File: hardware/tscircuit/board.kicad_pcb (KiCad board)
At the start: 2 copper layers, 240 x 180 mm, 133 parts, among them SW1 10mΩ, SW11 10mΩ, SW12 10mΩ, SW13 10mΩ

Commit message: hw(power/buses): fix 8 issues from schematic self-review (1 blocker)
An adversarial multi-agent review of the merged schematic surfaced 8 real
defects; each was verified against the combined netlist, then fixed:

- BLOCKER: +3V3 buck was TLV62569 (Vin max 5.5V) sitting on the 8.4V BAT node
  -> swapped to wide-Vin MP2315 (FB R3 45.3k->31.6k for 0.8V ref); EN auto-on
  via a 100k/47k divider off BAT instead of raw 8.4V on the EN pin.
- +5V and +3V3 MP2315 bootstrap caps (BST->SW) were missing -> bucks would not
  switch; added Cbst4 / Cbst5 100nF.
- S3 had no EN pin wired -> the reset chain (SW11 + RC) was a floating island;
  added U10.EN and connected net.S3_EN.
- C5 EN had no pull-up/RC -> undefined reset; added 10k + 1uF.
- USB VBUS missing bulk cap + TVS; added Cvbus 10uF + D1.
- RAIL_EN_5V / RAIL_EN_3V3A had no default state -> added 100k pull-downs (off).
- I2C had two pull-up pairs (~2.35k) -> removed the c5-buses pair, kept R40/R41.
- Grove ESD refdes off-by-one -> D40/D41 per the doc.

board.tsx re-merged (141 parts); power.md + power.ru.md synced.

Co-Authored-By: Claude Opus 4.8 <noreply@anthropic.com>
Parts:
- removed D40s: 10mΩ, tscircuit:resistor_res0603
- removed R_SCL, R_SDA: 4.7kΩ, tscircuit:resistor_res0402
- added C_C5EN: 1uF, tscircuit:capacitor_cap0402, F.Cu at (94.0, 110.7)
- added Cbst4: 100nF, tscircuit:capacitor_cap0402, F.Cu at (86.7, 76.1)
- added Cbst5: 100nF, tscircuit:capacitor_cap0402, F.Cu at (77.8, 74.6)
- added Cvbus: 10uF, tscircuit:capacitor_cap0805, F.Cu at (111.7, 121.0)
- added D1: 1MΩ, tscircuit:resistor_res0603, F.Cu at (115.1, 121.0)
- added D40: , tscircuit:chip_sot23-3, F.Cu at (79.8, 66.3)
- added R_C5EN: 10kΩ, tscircuit:resistor_res0402, F.Cu at (93.5, 108.3)
- added R_EN3H: 100kΩ, tscircuit:resistor_res0402, F.Cu at (72.9, 77.7)
- added R_EN3L: 47kΩ, tscircuit:resistor_res0402, F.Cu at (71.9, 80.5)
- added R_RE3A: 100kΩ, tscircuit:resistor_res0402, F.Cu at (106.2, 67.4)
- added R_RE5: 100kΩ, tscircuit:resistor_res0402, F.Cu at (94.1, 66.8)
- D42: value (none) -> 10mΩ; footprint tscircuit:chip_sot23-3 -> tscircuit:resistor_res0603
- R3: value 45.3kΩ -> 31.6kΩ
- moved D42 63.1 mm to (126.9, 103.9)
- moved Cd25 60.6 mm to (125.8, 75.4), turned to 0 degrees
- moved Cb22 56.6 mm to (126.5, 79.1)
- moved Cd23 56.4 mm to (123.4, 77.6)
- moved Cb25 53.1 mm to (120.4, 74.8), turned to -90 degrees
- moved Cd21 52.7 mm to (123.4, 80.5), turned to 90 degrees
- moved Cd22 52.2 mm to (121.0, 78.5), turned to 180 degrees
- moved Csd2 51.2 mm to (100.4, 124.6), turned to 180 degrees
- moved Cin3 45.9 mm to (91.9, 120.7)
- moved Cin5 44.5 mm to (95.6, 120.0), turned to 0 degrees
- moved Cd20 42.5 mm to (92.0, 110.7)
- moved Cjk2 34.9 mm to (97.9, 62.3), turned to 0 degrees
- moved SW13 32.3 mm to (100.0, 100.0)
- moved Cbulk31 31.9 mm to (68.9, 81.9), turned to -90 degrees
- moved Cvcc32 29.2 mm to (65.7, 76.9), turned to 90 degrees
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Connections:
- D42 pad 1: I2C_SDA -> V3V3
- D42 pad 2: I2C_SCL -> V_BCKP
- U10 pad 41: (no net) -> S3_EN
- U4 pad 1: (no net) -> .Cbst4 > .pin1 to .U4 > .BST
- U5 pad 1: .U5 > .SW to .L3 > .pin1 -> .Cbst5 > .pin1 to .U5 > .BST
- U5 pad 2: GND -> BAT
- U5 pad 3: .R3 > .pin2 to .U5 > .FB -> .U5 > .SW to .L3 > .pin1
- U5 pad 4: BAT -> GND
- U5 pad 5: BAT -> .R3 > .pin2 to .U5 > .FB
- U5 pad 6: (no net) -> .R_EN3H > .pin2 to .U5 > .EN
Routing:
- net GND: track 512.6 -> 0.00 mm, vias 50 -> 0
- net V3V3: track 321.6 -> 0.00 mm, vias 40 -> 0
- net V5: track 115.7 -> 0.00 mm, vias 12 -> 0
- net I2C_SDA: track 105.2 -> 0.00 mm, vias 14 -> 0
- net I2C_SCL: track 83.9 -> 0.00 mm, vias 14 -> 0
- net CC1101_RF: track 79.9 -> 0.00 mm, vias 4 -> 0
- net BAT: track 77.9 -> 0.00 mm, vias 12 -> 0
- net SPK_P: track 67.9 -> 0.00 mm, vias 2 -> 0
- net SPI_SCK: track 64.1 -> 0.00 mm, vias 12 -> 0
- net SPI_MOSI: track 63.8 -> 0.00 mm, vias 6 -> 0
- net SPI_MISO: track 62.6 -> 0.00 mm, vias 4 -> 0
- net GPS_UART_RX: track 57.0 -> 0.00 mm, vias 6 -> 0
- net .Cjk2 > .pin2 to .J30 > .R: track 46.5 -> 0.00 mm, vias 6 -> 0
- net LoRa_BUSY: track 45.3 -> 0.00 mm, vias 6 -> 0
- net nRF24_CE: track 45.2 -> 0.00 mm, vias 8 -> 0
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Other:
- board size 240 x 180 mm -> 250 x 180 mm

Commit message: hw(board): merge all 6 realized sheets into one real-parts board (169 parts)
Final recombine with the parts engine on: every sheet's real jlcpcb: footprints
carried into one board.tsx. Cross-sheet nets stitch (SPI / I2C / rails / CS /
interrupts / C5-link / SP4T-select all verified in board.net). KiCad DRC:
schematic_parity = 0, 0 shorts, 0 NaN. Refdes collisions renamed (U20, Y1, and the
new Rbias). The board is not yet routed (0 copper) — unconnected_items is the
ratsnest, not breaks; routing (RF by hand) is the next step. README updated.

Co-Authored-By: Claude Opus 4.8 <noreply@anthropic.com>
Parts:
- removed the D53 at (133.0, 92.6)
- removed the D54 at (69.5, 95.2)
- removed Rbias: 4.7kΩ, tscircuit:resistor_res0402
- removed the Rd52 at (133.6, 81.4)
- removed the Rd53 at (131.4, 94.8)
- added Cbat: 10uF, tscircuit:capacitor_cap0805, F.Cu at (65.2, 147.2)
- added Cbtst: 47nF, tscircuit:capacitor_cap0402, F.Cu at (77.7, 125.1)
- added Cbulk40: 10uF, tscircuit:capacitor_cap0805, F.Cu at (100.0, 100.0)
- added Cdc, Cds1, Cio40, Cu51, Cvcc40, Cvdd30b: 100nF, tscircuit:capacitor_cap0402, F.Cu at (100.0, 100.0)
- added Cpmid: 10uF, tscircuit:capacitor_cap0805, F.Cu at (124.0, 123.0)
- added Cregn: 4.7uF, tscircuit:capacitor_cap0805, F.Cu at (87.7, 149.1)
- added Csns: 47uF, tscircuit:capacitor_cap1210, F.Cu at (120.3, 130.8)
- added Cvbusic: 1uF, tscircuit:capacitor_cap0402, F.Cu at (115.8, 100.6)
- added Cvc: 0.1uF, tscircuit:capacitor_cap0402, F.Cu at (100.6, 163.5)
- added Cvcc4: 0.1uF, tscircuit:capacitor_cap0402, F.Cu at (80.4, 144.7)
- added Cvcc5: 0.1uF, tscircuit:capacitor_cap0402, F.Cu at (81.3, 157.7)
- added Cvdd: 0.1uF, tscircuit:capacitor_cap0402, F.Cu at (93.8, 165.5)
- added Q2: , tscircuit:chip, F.Cu at (93.0, 169.5)
- added Raam4: 100kΩ, tscircuit:resistor_res0402, F.Cu at (67.9, 142.1)
- added Raam5: 100kΩ, tscircuit:resistor_res0402, F.Cu at (57.6, 142.1)
- added Rcbset: 10Ω, tscircuit:resistor_res0402, F.Cu at (89.6, 137.0)
- added Ren: 10kΩ, tscircuit:resistor_res0402, F.Cu at (100.0, 100.0)
- added Rilim: 383Ω, tscircuit:resistor_res0402, F.Cu at (87.2, 137.0)
- added Rmid: 300Ω, tscircuit:resistor_res0402, F.Cu at (83.7, 156.2)
- added Rts_top: 5.23kΩ, tscircuit:resistor_res0402, F.Cu at (84.3, 137.0)
- added Rvc: 470Ω, tscircuit:resistor_res0402, F.Cu at (92.2, 163.1)
- added Rvdd: 470Ω, tscircuit:resistor_res0402, F.Cu at (81.3, 155.8)
- added Rvm: 2kΩ, tscircuit:resistor_res0402, F.Cu at (96.7, 168.1)
- added SW11, SW12, SW13: 10mΩ, tscircuit:resistor_res1210, F.Cu at (100.0, 100.0)
- added a_Rbias: 4.7kΩ, tscircuit:resistor_res0402, F.Cu at (100.0, 100.0)
- added rf_Rbias: 56kΩ, tscircuit:resistor_res0402, F.Cu at (100.0, 100.0)
- BL1: footprint tscircuit:chip_soic8 -> tscircuit:chip_soic6
- BT1: footprint tscircuit:chip_soic8 -> tscircuit:chip_pinrow3
- BT40: value 100000uF -> (none); footprint tscircuit:capacitor_cap1210 -> tscircuit:chip
- D40, D41: footprint tscircuit:chip_sot23-3 -> tscircuit:chip
- D42: value 10mΩ -> (none); footprint tscircuit:resistor_res0603 -> tscircuit:chip
- D53: renamed from Ren; value 10kΩ -> LED; footprint tscircuit:resistor_res0402 -> tscircuit:led_0603
- D54: renamed from SW13; value 10mΩ -> LED; footprint tscircuit:resistor_res1210 -> tscircuit:led_0603
- DS1, SW10, U27, U51: footprint tscircuit:chip_sot23-5 -> tscircuit:chip
- J1, J2, J40, J41, J50, Q1, U3, U4, U40, U5, U6: footprint tscircuit:chip_soic8 -> tscircuit:chip
- J30: footprint tscircuit:chip_soic8 -> tscircuit:chip_pinrow4
- Q50, Q51, Q52, Q53, Q54, Q55, Q56, Q57, Q58, U50: footprint tscircuit:chip_sot23 -> tscircuit:chip
- Rd52: renamed from SW11; value 10mΩ -> 4.7kΩ; footprint tscircuit:resistor_res1210 -> tscircuit:resistor_res0402
- Rd53: renamed from SW12; value 10mΩ -> 4.7kΩ; footprint tscircuit:resistor_res1210 -> tscircuit:resistor_res0402
- U10: footprint tscircuit:chip_qfn48 -> tscircuit:chip
- U11, U2, U23, U24, U25, U30, U31, m_U20: footprint tscircuit:chip_soic16 -> tscircuit:chip
- U12, U13: footprint tscircuit:chip_ssop24 -> tscircuit:chip
- U21, U22, rf_U20: footprint tscircuit:chip_soic8 -> tscircuit:chip_pinrow8_p2.54_doublerow
- U28, U32, U33: footprint tscircuit:chip_sot23-6 -> tscircuit:chip
- a_Y1: value 1mΩ -> (none); footprint tscircuit:resistor_res0402 -> tscircuit:chip
- rf_Y1: footprint tscircuit:crystal_cd3215 -> tscircuit:crystal_crystal_3215_2
- moved Q52 102.4 mm to (65.2, 163.3)
- moved D41 101.9 mm to (70.0, 163.4), turned to 0 degrees
- moved D40 98.7 mm to (88.5, 164.6), turned to -90 degrees
- moved Q53 98.2 mm to (64.3, 158.8)
- moved J41 95.9 mm to (79.4, 167.5), turned to 0 degrees
- moved U44 86.5 mm to (82.8, 151.5), turned to 180 degrees
- moved R3 85.0 mm to (84.2, 158.6), turned to 180 degrees
- moved J40 84.8 mm to (73.0, 154.3), turned to -90 degrees
- moved L3 82.0 mm to (64.5, 152.2), turned to -90 degrees
- moved R2 81.1 mm to (72.7, 146.3)
- moved Cout3a 81.0 mm to (45.0, 122.4), turned to 180 degrees
- moved R_RE3A 78.3 mm to (44.9, 116.1), turned to 180 degrees
- moved U22 76.5 mm to (97.4, 159.8), turned to 0 degrees
- moved BT1 75.1 mm to (79.4, 176.1), turned to 0 degrees
- moved R4 74.7 mm to (61.0, 150.4), turned to 180 degrees
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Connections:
- net .R_EN3H > .pin2 to .U5 > .EN renamed .R_EN3H > .pin2 to .U5 > .pin6
- BL1 pad 1: .U23 > .RFP to .BL1 > .RFP -> .U23 > .RF_P to .BL1 > .RFP
- BL1 pad 2: .U23 > .RFN to .BL1 > .RFN -> .U23 > .RF_N to .BL1 > .RFN
- BL1 pad 5: (no net) -> GND
- BL1 pad 6: (no net) -> GND
- BT1 pad 3: .BT1 > .P_MINUS to .Q1 > .D -> BMINUS
- CL1 pad 1: .U30 > .RCLK to .a_Y1 > .pin1 -> .U30 > .RCLK to .a_Y1 > .OSC1
- CL2 pad 1: GND -> .U30 > .RCLK to .a_Y1 > .OSC1
- Cx1 pad 1: .U23 > .XOSC1 to .rf_Y1 > .pin1 -> .U23 > .XOSC_Q1 to .rf_Y1 > .pin1
- Cx2 pad 1: .U23 > .XOSC2 to .rf_Y1 > .pin2 -> .U23 > .XOSC_Q2 to .rf_Y1 > .pin2
- D42 pad 2: V_BCKP -> (no net)
- D53 pad 1: V3V3 -> .D53 > .pin1 to .Rd53 > .pin1
- D53 pad 2: S3_EN -> .D53 > .pin2 to .Q53 > .C
- D54 pad 1: PTT_BTN -> .D54 > .pin1 to .Rd54 > .pin1
- D54 pad 2: GND -> .D54 > .pin2 to .Q54 > .C
- J1 pad 1: VBUS_S3 -> GND
- J1 pad 3: .Rcc1 > .pin1 to .J1 > .CC1 -> GND
- J1 pad 4: .Rcc2 > .pin1 to .J1 > .CC2 -> GND
- J1 pad 5: USB_DP_S3 -> GND
- J1 pad 6: USB_DM_S3 -> VBUS_S3
- J1 pad 7: (no net) -> .Rcc2 > .pin1 to .J1 > .CC2
- J2 pad 1: VBUS_C5 -> GND
- J2 pad 3: (no net) -> GND
- J2 pad 4: (no net) -> GND
- J2 pad 5: USB_DP_C5 -> GND
- J2 pad 6: USB_DM_C5 -> VBUS_C5
- J40 pad 1: V3V3 -> GND
- J40 pad 2: GND -> V3V3
- J40 pad 5: (no net) -> GND
- J40 pad 6: (no net) -> GND
- J41 pad 1: V3V3 -> GND
- J41 pad 2: GND -> V3V3
- J41 pad 5: (no net) -> GND
- J41 pad 6: (no net) -> GND
- J50 pad 1: SD_CS -> (no net)
- J50 pad 2: SPI_MOSI -> SD_CS
- J50 pad 3: SPI_MISO -> SPI_MOSI
- J50 pad 4: SPI_SCK -> V3V3
- J50 pad 5: V3V3 -> SPI_SCK
- J50 pad 7: SD_CD -> SPI_MISO
- L1 pad 1: .U2 > .SW to .L1 > .pin1 -> PMID
- L1 pad 2: BAT -> SW
- Q1 pad 1: .U3 > .DO to .Q1 > .G1 -> .U3 > .DO to .Q1 > .G
- Q1 pad 2: .U3 > .CO to .Q1 > .G2 -> BMINUS
- Q1 pad 3: .BT1 > .P_MINUS to .Q1 > .D -> PACKMID
- R_C5S27 pad 1: .m_U20 > .STRAP27 to .R_C5S27 > .pin1 -> .m_U20 > .IO27 to .R_C5S27 > .pin1
- Rd52 pad 1: S3_EN -> .D52 > .pin1 to .Rd52 > .pin1
- Rd52 pad 2: GND -> V3V3
- Rd53 pad 1: S3_BOOT -> .D53 > .pin1 to .Rd53 > .pin1
- Rd53 pad 2: GND -> V3V3
- Rin32 pad 2: .Rin32 > .pin2 to .U32 > .IN -> .Rin32 > .pin2 to .U32 > .IN_POS
- RsumL pad 1: .U30 > .LOUT to .RsumL > .pin1 -> .U30 > .pin2 to .RsumL > .pin1
- RsumR pad 1: .U30 > .ROUT to .RsumR > .pin1 -> .U30 > .pin1 to .RsumR > .pin1
- SW10 pad 4: ENC_SW -> GND
- SW10 pad 5: GND -> ENC_SW
- U10 pad 1: S3_BOOT -> GND
- U10 pad 10: HC138_B -> SA868_UART_RX
- U10 pad 11: HC138_C -> GPS_UART_RX
- U10 pad 12: SPI_MOSI -> HC138_A
- U10 pad 13: SPI_SCK -> USB_DM_S3
- U10 pad 14: SPI_MISO -> USB_DP_S3
- U10 pad 15: LCD_DC -> LoRa_DIO1
- U10 pad 16: LoRa_BUSY -> nRF24_IRQ
- U10 pad 17: SA868_UART_TX -> HC138_B
- U10 pad 18: SA868_UART_RX -> HC138_C
- U10 pad 19: GPS_UART_RX -> SPI_MOSI
- U10 pad 2: WS2812 -> V3V3
- U10 pad 20: USB_DM_S3 -> SPI_SCK
- U10 pad 21: USB_DP_S3 -> SPI_MISO
- U10 pad 22: LCD_TE -> LCD_DC
- U10 pad 23: C5_EN -> LCD_TE
- U10 pad 24: C5_BOOT -> GPS_UART_TX
- U10 pad 25: C5LINK_SCK -> PCA9555_INT
- U10 pad 26: C5LINK_MOSI -> CC1101_GDO2
- U10 pad 27: C5LINK_MISO -> S3_BOOT
- U10 pad 28: C5LINK_CS -> C5LINK_SCK
- U10 pad 29: C5LINK_DRDY -> C5LINK_MOSI
- U10 pad 3: IR_TX -> S3_EN
- U10 pad 30: ENC_A -> C5LINK_MISO
- U10 pad 31: ENC_B -> C5LINK_CS
- U10 pad 32: IR_RX -> C5LINK_DRDY
- U10 pad 33: C5_FLASH_TX -> ENC_A
- U10 pad 34: C5_FLASH_RX -> ENC_B
- U10 pad 35: CC1101_GDO2 -> IR_RX
- U10 pad 36: nRF24_IRQ -> C5_FLASH_RX
- U10 pad 37: GPS_UART_TX -> C5_FLASH_TX
- U10 pad 38: PCA9555_INT -> IR_TX
- U10 pad 39: V3V3 -> WS2812
- U10 pad 4: LoRa_DIO1 -> I2C_SDA
- U10 pad 41: S3_EN -> GND
- U10 pad 42: (no net) -> GND
- U10 pad 43: (no net) -> GND
- U10 pad 44: (no net) -> GND
- U10 pad 45: (no net) -> GND
- U10 pad 46: (no net) -> GND
- U10 pad 47: (no net) -> GND
- U10 pad 48: (no net) -> GND
- U10 pad 5: I2C_SDA -> I2C_SCL
- U10 pad 6: I2C_SCL -> nRF24_CE
- U10 pad 7: nRF24_CE -> CC1101_GDO0
- U10 pad 8: CC1101_GDO0 -> LoRa_BUSY
- U10 pad 9: HC138_A -> SA868_UART_TX
- U12 pad 1: ENC_SW -> PCA9555_INT
- U12 pad 10: BQ_INT -> LCD_RESX
- U12 pad 11: BQ_CD -> MUX_SEL
- U12 pad 12: LoRa_TR -> GND
- U12 pad 13: PAM_SD -> BQ_INT
- U12 pad 14: LCD_BL_EN -> BQ_CD
- U12 pad 15: RFSW_A -> LoRa_TR
- U12 pad 16: HC138_EN -> PAM_SD
- U12 pad 17: SD_CD -> LCD_BL_EN
- U12 pad 18: PCA9555_INT -> RFSW_A
- U12 pad 19: I2C_SCL -> HC138_EN
- U12 pad 2: SA868_PTT -> GND
- U12 pad 20: I2C_SDA -> SD_CD
- U12 pad 22: GND -> I2C_SCL
- U12 pad 23: GND -> I2C_SDA
- U12 pad 3: SA868_PD -> GND
- U12 pad 4: Si4732_RST -> ENC_SW
- U12 pad 5: LoRa_NRESET -> SA868_PTT
- U12 pad 6: BUZZER -> SA868_PD
- U12 pad 7: LCD_RESX -> Si4732_RST
- U12 pad 8: MUX_SEL -> LoRa_NRESET
- U12 pad 9: GND -> BUZZER
- U13 pad 1: PTT_BTN -> PCA9555_INT
- U13 pad 10: (no net) -> C5_BOOT
- U13 pad 11: (no net) -> RFSW_C
- U13 pad 12: (no net) -> GND
- U13 pad 18: PCA9555_INT -> (no net)
- U13 pad 19: I2C_SCL -> (no net)
- U13 pad 2: RAIL_EN_5V -> GND
- U13 pad 20: I2C_SDA -> (no net)
- U13 pad 22: GND -> I2C_SCL
- U13 pad 23: GND -> I2C_SDA
- U13 pad 3: RAIL_EN_3V3A -> GND
- U13 pad 4: JACK_DET -> PTT_BTN
- U13 pad 5: RFSW_B -> RAIL_EN_5V
- U13 pad 6: (no net) -> RAIL_EN_3V3A
- U13 pad 7: (no net) -> JACK_DET
- U13 pad 8: (no net) -> RFSW_B
- U13 pad 9: GND -> C5_EN
- U2 pad 1: VBUS_S3 -> (no net)
- U2 pad 10: GND -> .Rcbset > .pin1 to .U2 > .CBSET
- U2 pad 11: (no net) -> .Cregn > .pin1 to .U2 > .REGN
- U2 pad 12: (no net) -> .Cbtst > .pin1 to .U2 > .BTST
- U2 pad 13: (no net) -> BAT
- U2 pad 14: (no net) -> BAT
- U2 pad 15: (no net) -> BAT
- U2 pad 16: (no net) -> BAT
- U2 pad 2: .U2 > .SW to .L1 > .pin1 -> (no net)
- U2 pad 3: BAT -> BQ_CD
- U2 pad 4: BATM -> I2C_SDA
- U2 pad 5: TS -> I2C_SCL
- U2 pad 6: I2C_SDA -> BQ_INT
- U2 pad 7: I2C_SCL -> TS
- U2 pad 8: BQ_CD -> .Rilim > .pin1 to .U2 > .ILIM
- U2 pad 9: BQ_INT -> .Rmid > .pin1 to .U2 > .MID
- U23 pad 1: V3V3 -> SPI_SCK
- U23 pad 10: .U23 > .RFN to .BL1 > .RFN -> .U23 > .XOSC_Q2 to .rf_Y1 > .pin2
- U23 pad 11: .U23 > .XOSC1 to .rf_Y1 > .pin1 -> V3V3
- U23 pad 12: .U23 > .XOSC2 to .rf_Y1 > .pin2 -> .U23 > .RF_P to .BL1 > .RFP
- U23 pad 13: (no net) -> .U23 > .RF_N to .BL1 > .RFN
- U23 pad 14: (no net) -> V3V3
- U23 pad 15: (no net) -> V3V3
- U23 pad 16: (no net) -> GND
- U23 pad 2: GND -> SPI_MISO
- U23 pad 3: CC1101_CS -> CC1101_GDO2
- U23 pad 4: SPI_SCK -> V3V3
- U23 pad 5: SPI_MOSI -> .U23 > .DCOUPL to .Cdc > .pin1
- U23 pad 6: SPI_MISO -> CC1101_GDO0
- U23 pad 7: CC1101_GDO0 -> CC1101_CS
- U23 pad 8: CC1101_GDO2 -> .U23 > .XOSC_Q1 to .rf_Y1 > .pin1
- U23 pad 9: .U23 > .RFP to .BL1 > .RFP -> V3V3
- U24 pad 1: CC1101_RF -> GND
- U24 pad 10: (no net) -> .U24 > .RF4 to .Lm915 > .pin1
- U24 pad 11: (no net) -> GND
- U24 pad 12: (no net) -> GND
- U24 pad 13: (no net) -> CC1101_RF
- U24 pad 14: (no net) -> GND
- U24 pad 15: (no net) -> GND
- U24 pad 2: .U24 > .RF1 to .Lm315 > .pin1 -> .U24 > .RF3 to .Lm868 > .pin1
- U24 pad 3: .U24 > .RF2 to .Lm433 > .pin1 -> .U24 > .RF1 to .Lm315 > .pin1
- U24 pad 4: .U24 > .RF3 to .Lm868 > .pin1 -> V3V3
- U24 pad 5: .U24 > .RF4 to .Lm915 > .pin1 -> RFSW_C
- U24 pad 6: RFSW_A -> RFSW_B
- U24 pad 7: RFSW_B -> RFSW_A
- U24 pad 8: V3V3 -> GND
- U24 pad 9: GND -> .U24 > .RF2 to .Lm433 > .pin1
- U25 pad 1: V3V3 -> GND
- U25 pad 10: LoRa_RXEN -> GND
- U25 pad 11: LoRa_TR -> GND
- U25 pad 12: ANT_LoRa -> GND
- U25 pad 13: (no net) -> LoRa_DIO1
- U25 pad 14: (no net) -> LoRa_BUSY
- U25 pad 15: (no net) -> LoRa_NRESET
- U25 pad 16: (no net) -> SPI_MISO
- U25 pad 3: LoRa_NSS -> GND
- U25 pad 4: SPI_SCK -> GND
- U25 pad 5: SPI_MOSI -> GND
- U25 pad 6: SPI_MISO -> LoRa_RXEN
- U25 pad 7: LoRa_BUSY -> LoRa_TR
- U25 pad 8: LoRa_DIO1 -> (no net)
- U25 pad 9: LoRa_NRESET -> V3V3
- U27 pad 1: LoRa_TR -> (no net)
- U27 pad 2: LoRa_RXEN -> LoRa_TR
- U27 pad 3: V3V3 -> GND
- U27 pad 4: GND -> LoRa_RXEN
- U27 pad 5: (no net) -> V3V3
- U28 pad 2: nRF24_2_IRQ -> GND
- U28 pad 3: nRF24_3_IRQ -> nRF24_2_IRQ
- U28 pad 6: GND -> nRF24_3_IRQ
- U3 pad 1: BAT -> .U3 > .DO to .Q1 > .G
- U3 pad 2: BATM -> .U3 > .CO to .Q2 > .G
- U3 pad 3: .BT1 > .P_MINUS to .Q1 > .D -> .Rvm > .pin1 to .U3 > .VM
- U3 pad 4: .U3 > .DO to .Q1 > .G1 -> .Rvc > .pin1 to .U3 > .VC
- U3 pad 5: .U3 > .CO to .Q1 > .G2 -> .Rvdd > .pin1 to .U3 > .VDD
- U3 pad 6: (no net) -> BMINUS
- U30 pad 1: V3V3A -> .U30 > .pin1 to .RsumR > .pin1
- U30 pad 10: .U30 > .LOUT to .RsumL > .pin1 -> GND
- U30 pad 11: .U30 > .ROUT to .RsumR > .pin1 -> I2C_SCL
- U30 pad 12: (no net) -> I2C_SDA
- U30 pad 13: (no net) -> .U30 > .RCLK to .a_Y1 > .OSC1
- U30 pad 14: (no net) -> V3V3A
- U30 pad 15: (no net) -> GND
- U30 pad 2: GND -> .U30 > .pin2 to .RsumL > .pin1
- U30 pad 3: I2C_SDA -> (no net)
- U30 pad 4: I2C_SCL -> (no net)
- U30 pad 5: GND -> (no net)
- U30 pad 6: Si4732_RST -> ANT_FM
- U30 pad 7: .U30 > .RCLK to .a_Y1 > .pin1 -> GND
- U30 pad 9: ANT_FM -> Si4732_RST
- U31 pad 1: V5 -> GND
- U31 pad 10: ANT_UHF -> GND
- U31 pad 12: (no net) -> ANT_UHF
- U31 pad 16: (no net) -> SA868_UART_TX
- U31 pad 2: V3V3 -> (no net)
- U31 pad 3: GND -> SA_AF
- U31 pad 4: SA868_UART_TX -> (no net)
- U31 pad 5: SA868_UART_RX -> SA868_PTT
- U31 pad 6: SA868_PTT -> SA868_PD
- U31 pad 7: SA868_PD -> (no net)
- U31 pad 8: SA_AF -> V5
- U31 pad 9: .Cmic > .pin2 to .U31 > .MIC_IN -> GND
- U32 pad 1: .Rin32 > .pin2 to .U32 > .IN -> PAM_SD
- U32 pad 2: PAM_SD -> GND
- U32 pad 3: V5 -> .Rin32 > .pin2 to .U32 > .IN_POS
- U32 pad 4: GND -> (no net)
- U32 pad 6: SPK_M -> V5
- U33 pad 1: SI_AUDIO -> SA_AF
- U33 pad 2: SA_AF -> GND
- U33 pad 3: MUX_OUT -> SI_AUDIO
- U33 pad 4: MUX_SEL -> MUX_OUT
- U33 pad 6: GND -> MUX_SEL
- U4 pad 1: .Cbst4 > .pin1 to .U4 > .BST -> .Raam4 > .pin1 to .U4 > .AAM
- U4 pad 5: .R1 > .pin2 to .U4 > .FB -> .Cbst4 > .pin1 to .U4 > .BST
- U4 pad 7: (no net) -> .Cvcc4 > .pin1 to .U4 > .VCC
- U4 pad 8: (no net) -> .R1 > .pin2 to .U4 > .FB
- U40 pad 1: V3V3 -> GND
- U40 pad 2: GND -> V3V3
- U40 pad 3: GPS_UART_RX -> V_BCKP
- U40 pad 4: GPS_UART_TX -> GND
- U40 pad 5: V_BCKP -> GND
- U40 pad 6: (no net) -> GND
- U5 pad 1: .Cbst5 > .pin1 to .U5 > .BST -> .Raam5 > .pin1 to .U5 > .AAM
- U5 pad 5: .R3 > .pin2 to .U5 > .FB -> .Cbst5 > .pin1 to .U5 > .BST
- U5 pad 7: (no net) -> .Cvcc5 > .pin1 to .U5 > .VCC
- U5 pad 8: (no net) -> .R3 > .pin2 to .U5 > .FB
- U51 pad 1: WS2812 -> GND
- U51 pad 2: .U51 > .Y to .DS1 > .DIN -> WS2812
- U51 pad 4: V5 -> .U51 > .Y to .DS1 > .DIN
- U51 pad 5: GND -> V5
- U6 pad 4: V3V3A -> (no net)
- U6 pad 5: (no net) -> V3V3A
- a_Y1 pad 1: .U30 > .RCLK to .a_Y1 > .pin1 -> .U30 > .RCLK to .a_Y1 > .OSC1
- m_U20 pad 1: C5_EN -> GND
- m_U20 pad 10: C5_FLASH_RX -> C5LINK_CS
- m_U20 pad 11: C5_FLASH_TX -> C5LINK_DRDY
- m_U20 pad 12: USB_DM_C5 -> (no net)
- m_U20 pad 13: USB_DP_C5 -> USB_DM_C5
- m_U20 pad 14: V3V3 -> USB_DP_C5
- m_U20 pad 15: GND -> C5_BOOT
- m_U20 pad 2: C5_BOOT -> V3V3
- m_U20 pad 3: C5_BOOT -> C5_EN
- m_U20 pad 4: .m_U20 > .STRAP27 to .R_C5S27 > .pin1 -> (no net)
- m_U20 pad 5: C5LINK_SCK -> (no net)
- m_U20 pad 6: C5LINK_MOSI -> (no net)
- m_U20 pad 7: C5LINK_MISO -> (no net)
- m_U20 pad 8: C5LINK_CS -> C5LINK_MISO
- m_U20 pad 9: C5LINK_DRDY -> (no net)
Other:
- board size 250 x 180 mm -> 400 x 300 mm

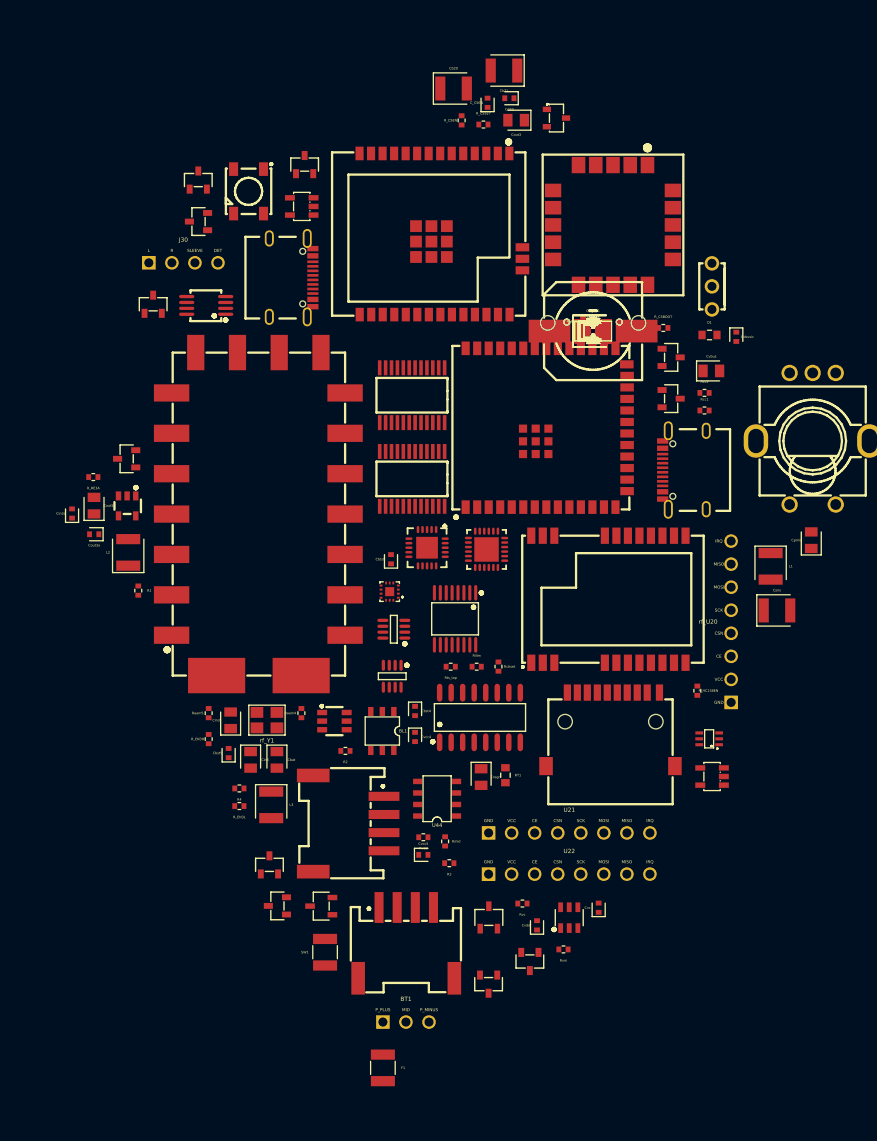
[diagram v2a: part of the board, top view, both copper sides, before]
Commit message: hw(board): re-merge after self-review fixes (174 parts, parity=0)
Re-combined all 6 corrected sheets. KiCad schematic_parity=0 (PCB netlist matches
schematic), 0 NaN. All 6 self-review fixes confirmed in the merged netlist: SNS
isolated from BAT, ESD cathodes on +3V3, PAM8302 input coupling caps, MP2315 20R
bootstraps, BQ25887 TS RT2. Cross-sheet buses stitch (SPI/I2C/rails/RFSW_C). The
board is unplaced/unrouted, so DRC unconnected + shorting are placement artifacts
(see README). README updated (174 parts + DRC note).

Co-Authored-By: Claude Opus 4.8 <noreply@anthropic.com>
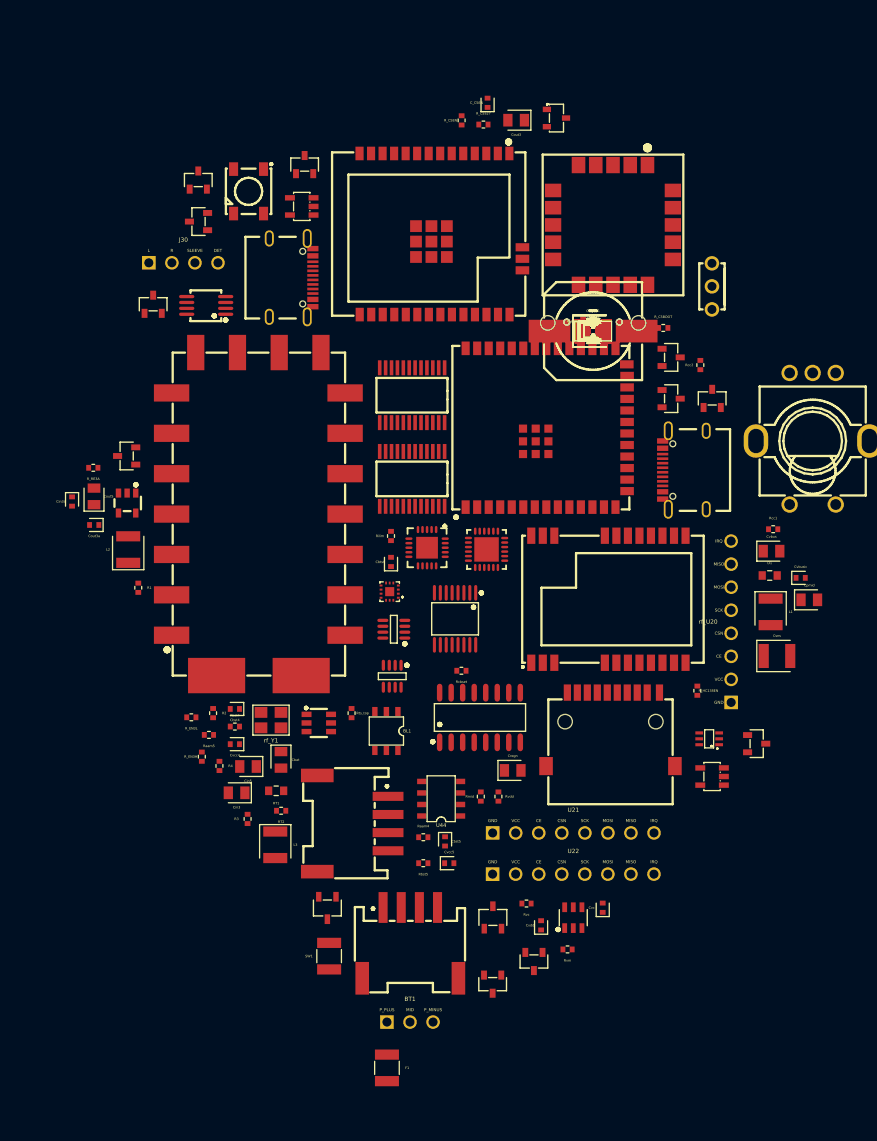
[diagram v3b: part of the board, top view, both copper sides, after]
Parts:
- removed the CL1 at (100.0, 100.0)
- removed the CL2 at (100.0, 100.0)
- removed the Cb20 at (84.6, 73.3)
- removed the Cb21 at (90.2, 71.3)
- removed the Cbulk40 at (100.0, 100.0)
- removed the Cd20 at (90.8, 74.3)
- removed the Cdc at (100.0, 100.0)
- removed the Cir at (100.0, 100.0)
- removed the Csd1 at (100.0, 100.0)
- removed the Cu51 at (100.0, 100.0)
- removed the Cvdd30 at (100.0, 100.0)
- removed the Cx1 at (100.0, 100.0)
- removed the D50 at (100.0, 100.0)
- removed the D51 at (100.0, 100.0)
- removed the D52 at (100.0, 100.0)
- removed the D53 at (100.0, 100.0)
- removed the D54 at (100.0, 100.0)
- removed the D55 at (100.0, 100.0)
- removed the D56 at (100.0, 100.0)
- removed the LS1 at (100.0, 100.0)
- removed the Lm868 at (100.0, 100.0)
- added Cb22: 150uF, tscircuit:capacitor_cap1210, F.Cu at (100.0, 100.0)
- added Cb25: 100uF, tscircuit:capacitor_cap1210, F.Cu at (100.0, 100.0)
- added Cd21, Cd22, Cd25, Cds1, Cio40, Cvdd30b: 100nF, tscircuit:capacitor_cap0402, F.Cu at (100.0, 100.0)
- added Cen: 1uF, tscircuit:capacitor_cap0402, F.Cu at (100.0, 100.0)
- added Cjk2: 220uF, tscircuit:capacitor_cap1210, F.Cu at (100.0, 100.0)
- added LS2, SW11, SW12: 10mΩ, tscircuit:resistor_res1210, F.Cu at (100.0, 100.0)
- added Lm433: 1nH, tscircuit:inductor_0402, F.Cu at (100.0, 100.0)
- added R40, R41, Rd51, Rd52, Rd53, Rd54, Rd55, a_Rbias: 4.7kΩ, tscircuit:resistor_res0402, F.Cu at (100.0, 100.0)
- added RT2: 30.1kΩ, tscircuit:resistor_res0402, F.Cu at (65.6, 152.9)
- added Rbst4: 20Ω, tscircuit:resistor_res0402, F.Cu at (60.5, 143.6)
- added Rbst5: 20Ω, tscircuit:resistor_res0402, F.Cu at (81.3, 158.6)
- added Rin32: 10kΩ, tscircuit:resistor_res0402, F.Cu at (100.0, 100.0)
- CL1: renamed from Cvdd30b; value 100nF -> 12pF
- CL2: renamed from RsumL; value 10kΩ -> 12pF; footprint tscircuit:resistor_res0402 -> tscircuit:capacitor_cap0402
- Cb20: renamed from Cd21; value 100nF -> 150uF; footprint tscircuit:capacitor_cap0402 -> tscircuit:capacitor_cap1210
- Cb21: renamed from Cd22; value 100nF -> 150uF; footprint tscircuit:capacitor_cap0402 -> tscircuit:capacitor_cap1210
- Cb23: renamed from Lm315; value 1nH -> 100uF; footprint tscircuit:inductor_0402 -> tscircuit:capacitor_cap1210
- Cbulk31: renamed from a_Rbias; value 4.7kΩ -> 330uF; footprint tscircuit:resistor_res0402 -> tscircuit:capacitor_cap1210
- Cbulk40: renamed from R41; value 4.7kΩ -> 10uF; footprint tscircuit:resistor_res0402 -> tscircuit:capacitor_cap0805
- Cbyp31: renamed from Cmic; value 1uF -> 100nF
- Cd20: renamed from Cb22; value 150uF -> 100nF; footprint tscircuit:capacitor_cap1210 -> tscircuit:capacitor_cap0402
- Cd23: renamed from Lm433; value 1nH -> 100nF; footprint tscircuit:inductor_0402 -> tscircuit:capacitor_cap0402
- Cdc: renamed from Cb23; value 100uF -> 100nF; footprint tscircuit:capacitor_cap1210 -> tscircuit:capacitor_cap0402
- Cinn: renamed from Cjk2; value 220uF -> 0.1uF; footprint tscircuit:capacitor_cap1210 -> tscircuit:capacitor_cap0402
- Cinp: renamed from Cjk1; value 220uF -> 0.1uF; footprint tscircuit:capacitor_cap1210 -> tscircuit:capacitor_cap0402
- Cir: renamed from SW11; value 10mΩ -> 100nF; footprint tscircuit:resistor_res1210 -> tscircuit:capacitor_cap0402
- Cjk1: renamed from Cio40; value 100nF -> 220uF; footprint tscircuit:capacitor_cap0402 -> tscircuit:capacitor_cap1210
- Cmic: renamed from Rin32; value 10kΩ -> 1uF; footprint tscircuit:resistor_res0402 -> tscircuit:capacitor_cap0402
- Csd1: renamed from Cen; value 1uF -> 10uF; footprint tscircuit:capacitor_cap0402 -> tscircuit:capacitor_cap0805
- Csd2: renamed from SW12; value 10mΩ -> 100nF; footprint tscircuit:resistor_res1210 -> tscircuit:capacitor_cap0402
- Cu51: renamed from Rir; value 47Ω -> 100nF; footprint tscircuit:resistor_res0603 -> tscircuit:capacitor_cap0402
- Cvcc40: renamed from R40; value 4.7kΩ -> 100nF; footprint tscircuit:resistor_res0402 -> tscircuit:capacitor_cap0402
- Cvdd30: renamed from RsumR; value 10kΩ -> 1uF; footprint tscircuit:resistor_res0402 -> tscircuit:capacitor_cap0402
- Cx1: renamed from rf_Rbias; value 56kΩ -> 10pF; footprint tscircuit:resistor_res0402 -> tscircuit:capacitor_cap0402
- D50: renamed from Rd51; value 4.7kΩ -> LED; footprint tscircuit:resistor_res0402 -> tscircuit:led_0603
- D51: renamed from Rd52; value 4.7kΩ -> LED; footprint tscircuit:resistor_res0402 -> tscircuit:led_0603
- D52: renamed from Rd53; value 4.7kΩ -> LED; footprint tscircuit:resistor_res0402 -> tscircuit:led_0603
- D53: renamed from Rd54; value 4.7kΩ -> LED; footprint tscircuit:resistor_res0402 -> tscircuit:led_0603
- D54: renamed from Rd55; value 4.7kΩ -> LED; footprint tscircuit:resistor_res0402 -> tscircuit:led_0603
- D55: renamed from Rd56; value 4.7kΩ -> LED; footprint tscircuit:resistor_res0402 -> tscircuit:led_0603
- D56: renamed from Cds1; value 100nF -> LED; footprint tscircuit:capacitor_cap0402 -> tscircuit:led_0603
- LS1: renamed from Cvcc40; value 100nF -> 4Ω; footprint tscircuit:capacitor_cap0402 -> tscircuit:resistor_res1210
- Lm868: renamed from Cb25; value 100uF -> 1nH; footprint tscircuit:capacitor_cap1210 -> tscircuit:inductor_0402
- Lm915: renamed from Cd25; value 100nF -> 1nH; footprint tscircuit:capacitor_cap0402 -> tscircuit:inductor_0402
- Rd56: renamed from LS2; value 10mΩ -> 4.7kΩ; footprint tscircuit:resistor_res1210 -> tscircuit:resistor_res0402
- Rir: renamed from Csd2; value 100nF -> 47Ω; footprint tscircuit:capacitor_cap0402 -> tscircuit:resistor_res0603
- RsumL: renamed from Cbulk31; value 330uF -> 10kΩ; footprint tscircuit:capacitor_cap1210 -> tscircuit:resistor_res0402
- RsumR: renamed from Cbyp31; value 100nF -> 10kΩ; footprint tscircuit:capacitor_cap0402 -> tscircuit:resistor_res0402
- rf_Rbias: renamed from Cd23; value 100nF -> 56kΩ; footprint tscircuit:capacitor_cap0402 -> tscircuit:resistor_res0402
- moved Q56 87.4 mm to (118.0, 145.5), turned to 180 degrees
- moved Q53 71.3 mm to (56.5, 87.9), turned to 0 degrees
- moved Q52 67.7 mm to (51.5, 97.0), turned to -90 degrees
- moved Q55 59.9 mm to (113.1, 107.4), turned to -90 degrees
- moved Cvbusic 27.5 mm to (122.9, 127.2), turned to 0 degrees
- moved D1 27.3 mm to (119.5, 126.9)
- moved Cbst5 25.8 mm to (83.7, 156.2), turned to -90 degrees
- moved RT1 25.3 mm to (65.1, 150.7), turned to 180 degrees
- moved R3 22.8 mm to (61.9, 153.8), turned to 90 degrees
- moved Cvbus 20.9 mm to (119.7, 124.3)
- moved Cvcc4 19.9 mm to (60.5, 145.5), turned to 180 degrees
- moved Cbst4 19.9 mm to (60.5, 141.6), turned to 180 degrees
- moved Raam4 19.2 mm to (81.3, 155.8), turned to 0 degrees
- moved Rilim 17.2 mm to (77.7, 122.6), turned to 90 degrees
- moved R2 15.2 mm to (58.1, 142.1), turned to -90 degrees
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- renumbered Lm915 to Lm315
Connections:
- CL1 pad 1: V3V3A -> .U30 > .RCLK to .a_Y1 > .OSC1
- CL2 pad 1: .U30 > .pin2 to .RsumL > .pin1 -> .U30 > .RCLK to .a_Y1 > .OSC1
- CL2 pad 2: SI_AUDIO -> GND
- Cb23 pad 1: .U24 > .RF1 to .Lm315 > .pin1 -> V3V3
- Cb23 pad 2: ANT_CC1101 -> GND
- Cbst4 pad 2: .U4 > .SW to .L2 > .pin1 -> .Cbst4 > .pin2 to .Rbst4 > .pin1
- Cbst5 pad 2: .U5 > .SW to .L3 > .pin1 -> .Cbst5 > .pin2 to .Rbst5 > .pin1
- Cbulk31 pad 1: V3V3A -> V5
- Cbulk31 pad 2: MIC_HOT -> GND
- Cbulk40 pad 2: I2C_SCL -> GND
- Cbyp31 pad 1: MIC_HOT -> V5
- Cbyp31 pad 2: .Cmic > .pin2 to .U31 > .MIC_IN -> GND
- Cd23 pad 1: .U24 > .RF2 to .Lm433 > .pin1 -> V3V3
- Cd23 pad 2: ANT_CC1101 -> GND
- Cdc pad 1: V3V3 -> .U23 > .DCOUPL to .Cdc > .pin1
- Cinn pad 1: SPK_M -> .U32 > .IN_NEG to .Cinn > .pin1
- Cinn pad 2: .Cjk2 > .pin2 to .J30 > .R -> GND
- Cinp pad 1: SPK_P -> .Rin32 > .pin2 to .Cinp > .pin1
- Cinp pad 2: .Cjk1 > .pin2 to .J30 > .L -> .Cinp > .pin2 to .U32 > .IN_POS
- Cir pad 1: S3_EN -> V3V3
- Cjk1 pad 1: V3V3 -> SPK_P
- Cjk1 pad 2: GND -> .Cjk1 > .pin2 to .J30 > .L
- Cmic pad 1: MUX_OUT -> MIC_HOT
- Cmic pad 2: .Rin32 > .pin2 to .U32 > .IN_POS -> .Cmic > .pin2 to .U31 > .MIC_IN
- Csd1 pad 1: S3_EN -> V3V3
- Csd2 pad 1: S3_BOOT -> V3V3
- Csns pad 1: BAT -> SNS
- Cu51 pad 1: .D57 > .pin1 to .Rir > .pin1 -> V5
- Cu51 pad 2: V5 -> GND
- Cvcc40 pad 2: I2C_SDA -> GND
- Cvdd30 pad 1: .U30 > .pin1 to .RsumR > .pin1 -> V3V3A
- Cvdd30 pad 2: SI_AUDIO -> GND
- Cx1 pad 1: .U23 > .RBIAS to .rf_Rbias > .pin1 -> .U23 > .XOSC_Q1 to .rf_Y1 > .pin1
- D40 pad 3: GND -> V3V3
- D41 pad 3: GND -> V3V3
- D50 pad 1: .D51 > .pin1 to .Rd51 > .pin1 -> .D50 > .pin1 to .Rd50 > .pin1
- D50 pad 2: V3V3 -> .D50 > .pin2 to .Q50 > .C
- D51 pad 1: .D52 > .pin1 to .Rd52 > .pin1 -> .D51 > .pin1 to .Rd51 > .pin1
- D51 pad 2: V3V3 -> .D51 > .pin2 to .Q51 > .C
- D52 pad 1: .D53 > .pin1 to .Rd53 > .pin1 -> .D52 > .pin1 to .Rd52 > .pin1
- D52 pad 2: V3V3 -> .D52 > .pin2 to .Q52 > .C
- D53 pad 1: .D54 > .pin1 to .Rd54 > .pin1 -> .D53 > .pin1 to .Rd53 > .pin1
- D53 pad 2: V3V3 -> .D53 > .pin2 to .Q53 > .C
- D54 pad 1: .D55 > .pin1 to .Rd55 > .pin1 -> .D54 > .pin1 to .Rd54 > .pin1
- D54 pad 2: V3V3 -> .D54 > .pin2 to .Q54 > .C
- D55 pad 1: .D56 > .pin1 to .Rd56 > .pin1 -> .D55 > .pin1 to .Rd55 > .pin1
- D55 pad 2: V3V3 -> .D55 > .pin2 to .Q55 > .C
- D56 pad 1: V5 -> .D56 > .pin1 to .Rd56 > .pin1
- D56 pad 2: GND -> .D56 > .pin2 to .Q56 > .C
- LS1 pad 1: V3V3 -> SPK_P
- LS1 pad 2: GND -> SPK_M
- Lm315 pad 1: .U24 > .RF4 to .Lm915 > .pin1 -> .U24 > .RF1 to .Lm315 > .pin1
- Lm868 pad 1: V3V3 -> .U24 > .RF3 to .Lm868 > .pin1
- Lm868 pad 2: GND -> ANT_CC1101
- Lm915 pad 1: V3V3 -> .U24 > .RF4 to .Lm915 > .pin1
- Lm915 pad 2: GND -> ANT_CC1101
- Rd56 pad 1: V5 -> .D56 > .pin1 to .Rd56 > .pin1
- Rd56 pad 2: .LS2 > .pin2 to .Q57 > .C -> V3V3
- Rir pad 1: V3V3 -> .D57 > .pin1 to .Rir > .pin1
- Rir pad 2: GND -> V5
- RsumL pad 1: V5 -> .U30 > .pin2 to .RsumL > .pin1
- RsumL pad 2: GND -> SI_AUDIO
- RsumR pad 1: V5 -> .U30 > .pin1 to .RsumR > .pin1
- RsumR pad 2: GND -> SI_AUDIO
- U2 pad 15: BAT -> SNS
- U2 pad 16: BAT -> SNS
- U24 pad 1: GND -> (no net)
- U24 pad 11: GND -> (no net)
- U24 pad 12: GND -> (no net)
- U24 pad 14: GND -> (no net)
- U24 pad 8: GND -> (no net)
- U32 pad 2: GND -> .U32 > .IN_NEG to .Cinn > .pin1
- U32 pad 3: .Rin32 > .pin2 to .U32 > .IN_POS -> .Cinp > .pin2 to .U32 > .IN_POS
- rf_Rbias pad 1: V3V3 -> .U23 > .RBIAS to .rf_Rbias > .pin1
